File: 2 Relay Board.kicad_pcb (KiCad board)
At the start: 2 copper layers, 158 x 75 mm, 44 parts, among them J1 Conn_01x02, J2 Conn_01x03, J3 Conn_01x05, K1 RAYEX-L90, K2 RAYEX-L90, Q1 BD139, Q2 BD139, U1 N76E003, U2 LM2936-5.0_TO92, U3 LM7812_TO220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

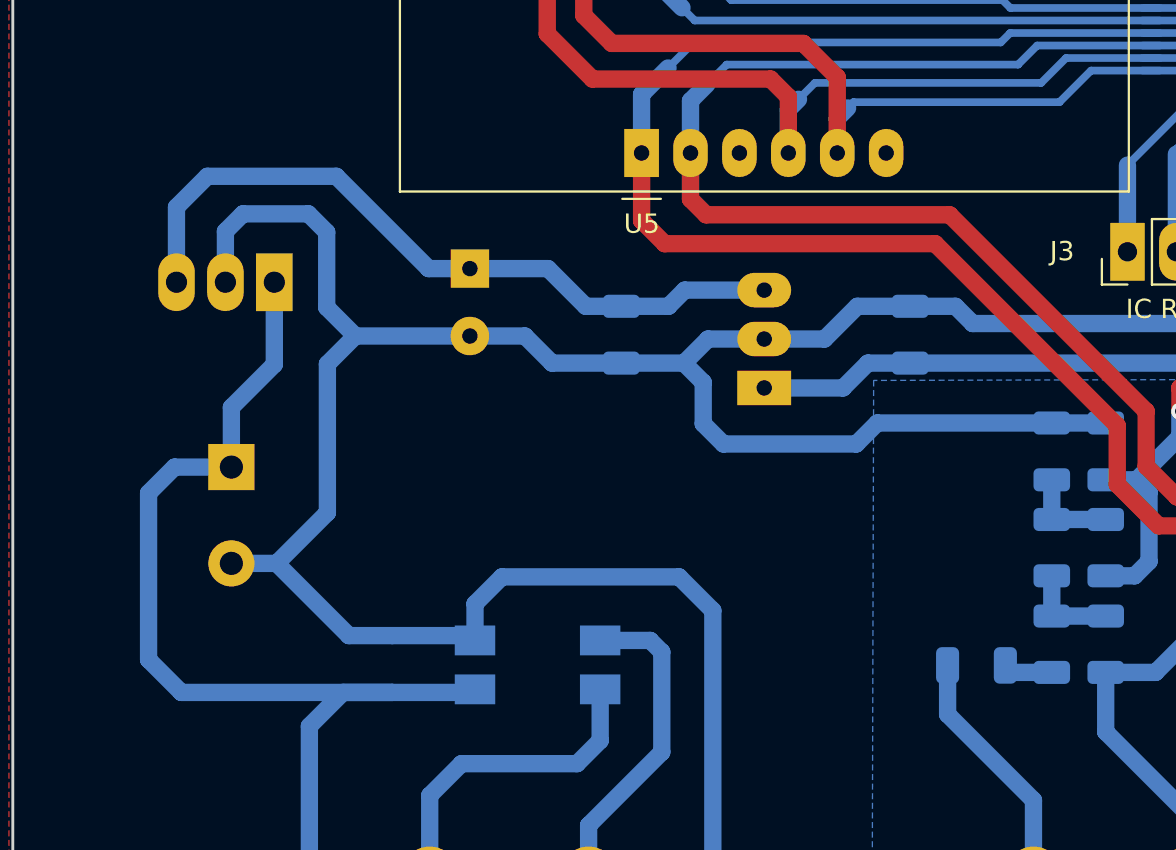
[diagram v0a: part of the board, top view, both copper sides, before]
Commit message: this version hase smd LDO v1.2
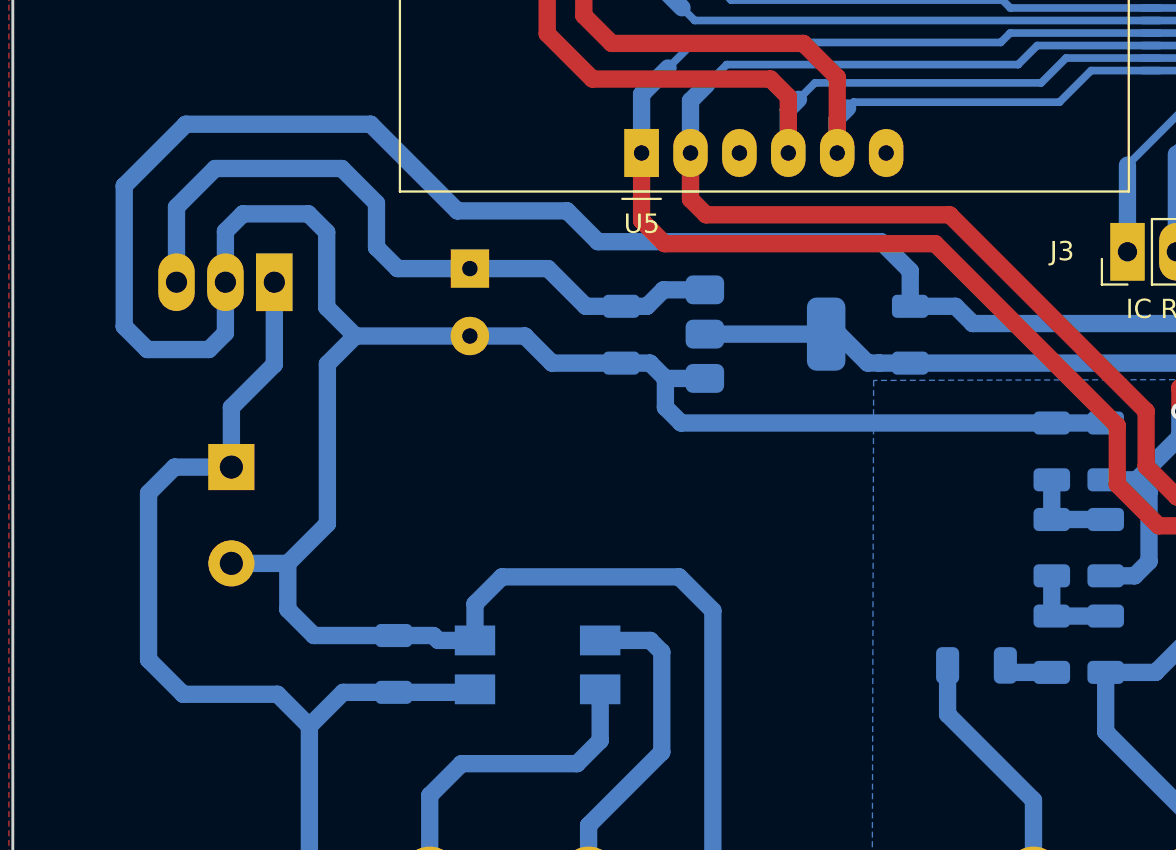
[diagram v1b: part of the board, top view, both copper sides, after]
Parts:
- removed U2: LM2936-5.0_TO92, My Custom Footprint:TO-92_Inline_Wide_LM78L05
- added C3: 0.1uf/50v, My Custom Footprint:C_1206_3216Metric, B.Cu at (91.5, 115.9)
- added U4: AMS1117-5.0, Package_TO_SOT_SMD:SOT-223-3_TabPin2, B.Cu at (110.8, 98.8)
- C1, C12, C2, C6, C8: value C -> 10uf/50v
- C10, C5, C7: value C -> 0.1uf/50v
- U3: value LM7812_TO220 -> LM7809_TO220
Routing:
- net VSS: track 318.0 -> 370.5 mm
- net +24V: track 277.2 -> 273.8 mm
- net VDD: track 47.6 -> 50.8 mm
- net +12V: track 38.2 -> 36.8 mm

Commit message: this version hase small 7805 v1.1
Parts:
- removed C3: 0.1uf/50v, My Custom Footprint:C_1206_3216Metric
- removed U4: AMS1117-5.0, Package_TO_SOT_SMD:SOT-223-3_TabPin2
- added U2: LM2936-5.0_TO92, My Custom Footprint:TO-92_Inline_Wide_LM78L05, B.Cu at (110.8, 101.6)
- C1, C12, C2, C6, C8: value 10uf/50v -> C
- C10, C5, C7: value 0.1uf/50v -> C
- U3: value LM7809_TO220 -> LM7812_TO220
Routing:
- net VSS: track 370.5 -> 318.0 mm
- net +24V: track 273.8 -> 277.2 mm
- net VDD: track 50.8 -> 47.6 mm
- net +12V: track 36.8 -> 38.2 mm
